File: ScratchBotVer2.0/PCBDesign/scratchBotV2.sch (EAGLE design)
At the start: 55 parts, among them T1 BD139, T3 BD139, U1 LM358M/NOPB, U2 LM358M/NOPB, U3 TCRT5000, U4 TCRT5000

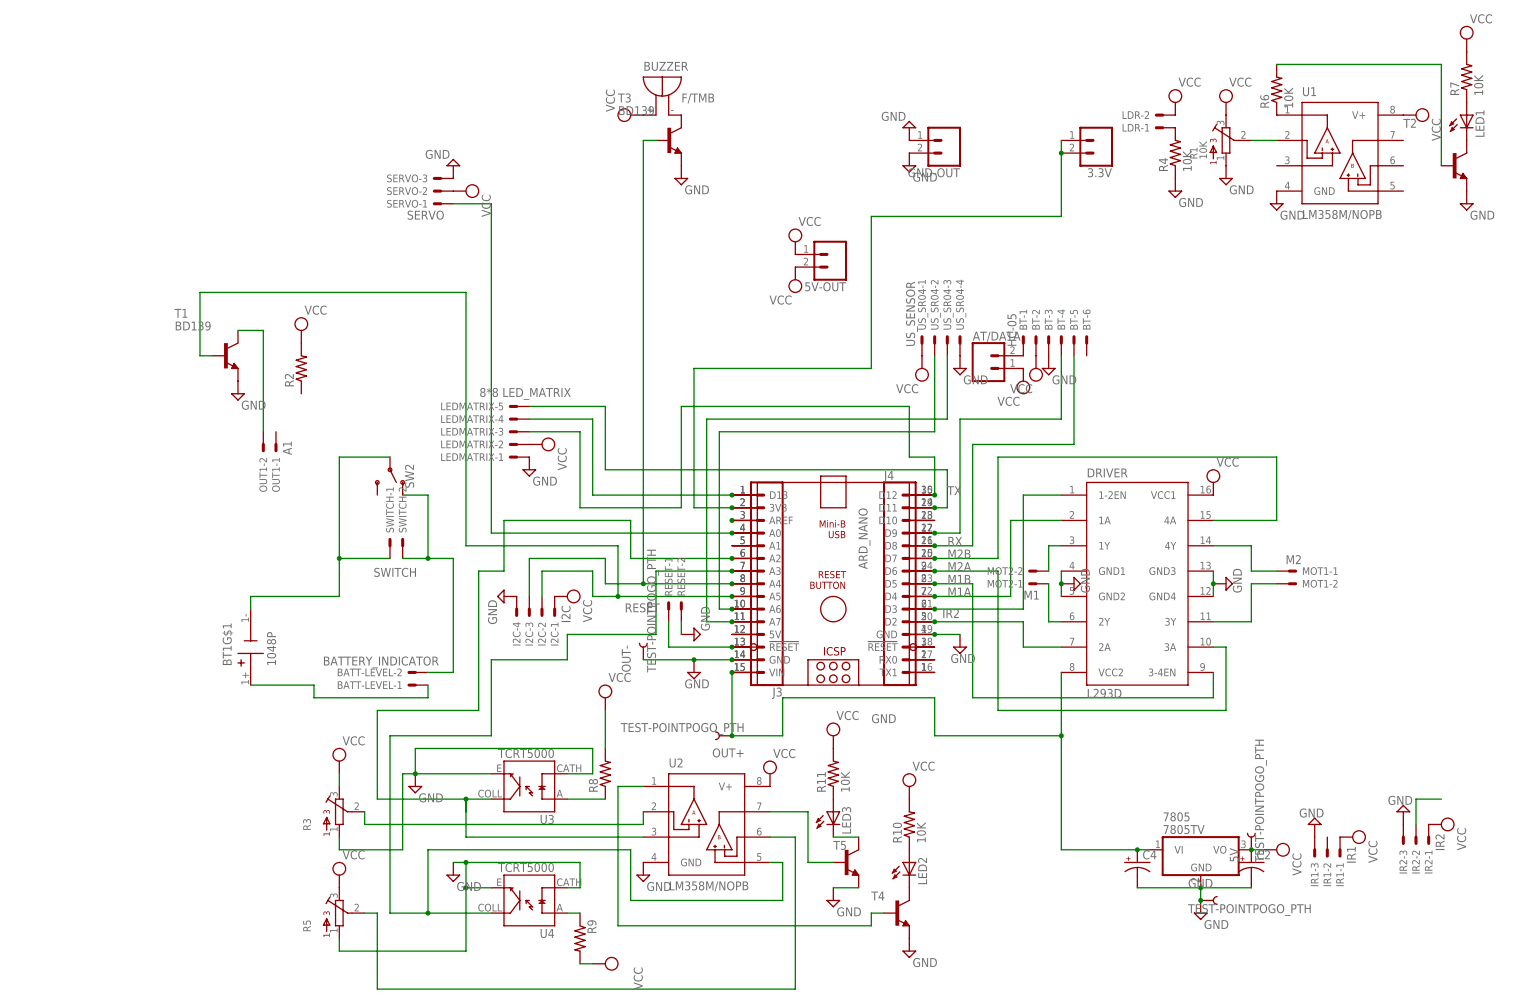
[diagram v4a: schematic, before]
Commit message: Output Pins of TCR5000 and LDR is connected to the analog pin of Arduino and reviewed the circuit.
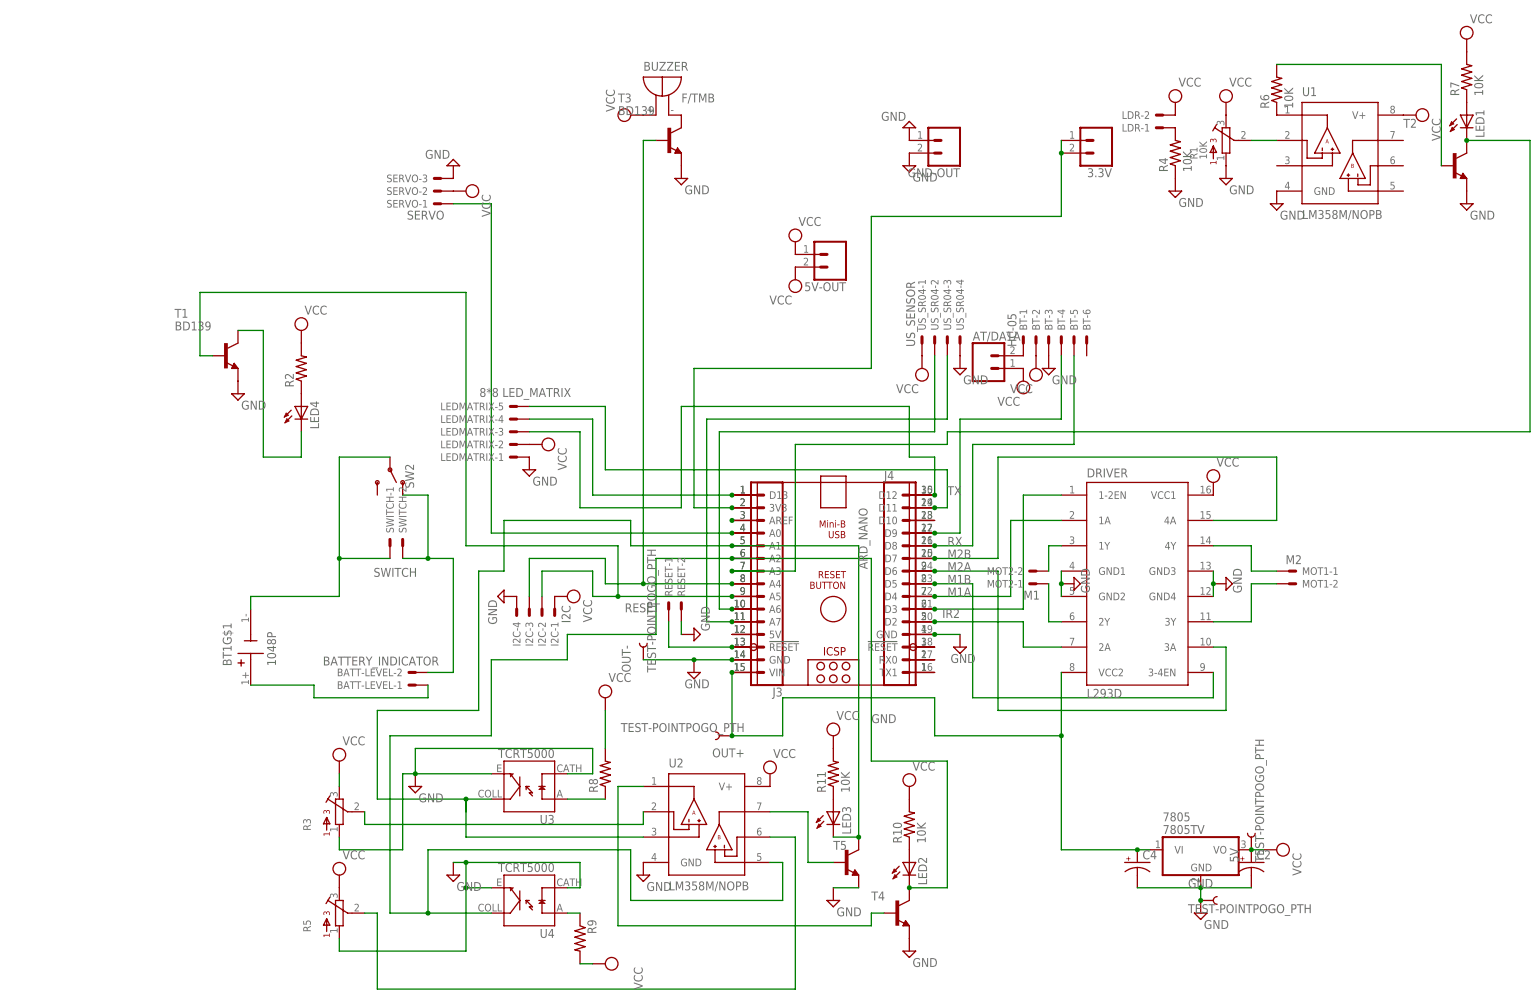
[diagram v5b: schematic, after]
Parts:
- removed IR1: IR1, Rembrandt Electronics - JST XH Connectors v1-0 (1):JST-XH-03-PIN-LONG-PAD
- removed IR2: IR2, Rembrandt Electronics - JST XH Connectors v1-0 (1):JST-XH-03-PIN-LONG-PAD
- removed OUT1: A1, Rembrandt Electronics - JST XH Connectors v1-0 (1):JST-XH-02-PIN-LONG-PAD
- added LED4: (no value), adafruit:LEDCHIPLED_1206
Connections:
- removed net N$30: LED2.C, T4.C
- removed net N$40: IR2-2.S
- removed net N$41: ARD_NANO.A3, J3.7, U2.+INB, U4.COLL
- removed net N$46: LED3.C, T5.C
- new net N$49: LED4.A, R2.1
- net GND: no longer IR1-3.S, IR2-3.S
- net N$15: now also ARD_NANO.A3, J3.7, LED1.C, T2.C; no longer ARD_NANO.A1, J3.5
- net N$16: now also ARD_NANO.A1, J3.5, LED3.C, T5.C; no longer ARD_NANO.A2, J3.6
- net N$17: now also LED4.C; no longer OUT1-2.S
- net N$32: now also ARD_NANO.A2, J3.6, LED2.C, T4.C, U2.+INB, U4.COLL; no longer LED1.C, T2.C
- net VCC: no longer IR1-1.S, IR2-1.S

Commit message: Resistors value updated
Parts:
- R10, R11: value 10K -> 100E
- R3, R5: value (none) -> 10K
- R7: value 10K -> 330 ohm
- R8, R9: value (none) -> 150 ohm
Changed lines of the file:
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@@
 <part name="U2" library="LM358M_NOPB" deviceset="LM358M/NOPB" device=""/>
 <part name="R1" library="bourns" deviceset="3362" device="H" value="10K"/>
-<part name="R3" library="bourns" deviceset="3362" device="H"/>
+<part name="R3" library="bourns" deviceset="3362" device="H" value="10K"/>
 <part name="SUPPLY32" library="supply2" library_urn="urn:adsk.eagle:library:372" deviceset="GND" device=""/>
 <part name="SUPPLY33" library="supply2" library_urn="urn:adsk.eagle:library:372" deviceset="VCC" device=""/>
@@
 <part name="SUPPLY38" library="supply2" library_urn="urn:adsk.eagle:library:372" deviceset="GND" device=""/>
 <part name="LED1" library="adafruit" deviceset="LED" device="CHIPLED_1206"/>
-<part name="R7" library="adafruit" deviceset="R-US_" device="M1206" value="10K"/>
+<part name="R7" library="adafruit" deviceset="R-US_" device="M1206" value="330 ohm"/>
 <part name="SUPPLY39" library="supply2" library_urn="urn:adsk.eagle:library:372" deviceset="VCC" device=""/>
 <part name="SUPPLY19" library="supply2" library_urn="urn:adsk.eagle:library:372" deviceset="GND" device=""/>
@@
 <part name="U4" library="TCRT5000" deviceset="TCRT5000" device=""/>
 <part name="SUPPLY40" library="supply2" library_urn="urn:adsk.eagle:library:372" deviceset="GND" device=""/>
-<part name="R8" library="adafruit" deviceset="R-US_" device="M1206"/>
+<part name="R8" library="adafruit" deviceset="R-US_" device="M1206" value="150 ohm"/>
 <part name="SUPPLY41" library="supply2" library_urn="urn:adsk.eagle:library:372" deviceset="VCC" device=""/>
-<part name="R9" library="adafruit" deviceset="R-US_" device="M1206"/>
+<part name="R9" library="adafruit" deviceset="R-US_" device="M1206" value="150 ohm"/>
 <part name="SUPPLY42" library="supply2" library_urn="urn:adsk.eagle:library:372" deviceset="VCC" device=""/>
 <part name="SUPPLY43" library="supply2" library_urn="urn:adsk.eagle:library:372" deviceset="GND" device=""/>
 <part name="SUPPLY44" library="supply2" library_urn="urn:adsk.eagle:library:372" deviceset="GND" device=""/>
 <part name="LED2" library="adafruit" deviceset="LED" device="CHIPLED_1206"/>
-<part name="R10" library="adafruit" deviceset="R-US_" device="M1206" value="10K"/>
+<part name="R10" library="adafruit" deviceset="R-US_" device="M1206" value="100E"/>
 <part name="SUPPLY45" library="supply2" library_urn="urn:adsk.eagle:library:372" deviceset="VCC" device=""/>
 <part name="SUPPLY46" library="supply2" library_urn="urn:adsk.eagle:library:372" deviceset="GND" device=""/>
@@
 <part name="SUPPLY48" library="supply2" library_urn="urn:adsk.eagle:library:372" deviceset="GND" device=""/>
 <part name="LED3" library="adafruit" deviceset="LED" device="CHIPLED_1206"/>
-<part name="R11" library="adafruit" deviceset="R-US_" device="M1206" value="10K"/>
+<part name="R11" library="adafruit" deviceset="R-US_" device="M1206" value="100E"/>
 <part name="SUPPLY49" library="supply2" library_urn="urn:adsk.eagle:library:372" deviceset="VCC" device=""/>
-<part name="R5" library="bourns" deviceset="3362" device="H"/>
+<part name="R5" library="bourns" deviceset="3362" device="H" value="10K"/>
 <part name="SUPPLY50" library="supply2" library_urn="urn:adsk.eagle:library:372" deviceset="VCC" device=""/>
 <part name="SUPPLY51" library="supply2" library_urn="urn:adsk.eagle:library:372" deviceset="VCC" device=""/>

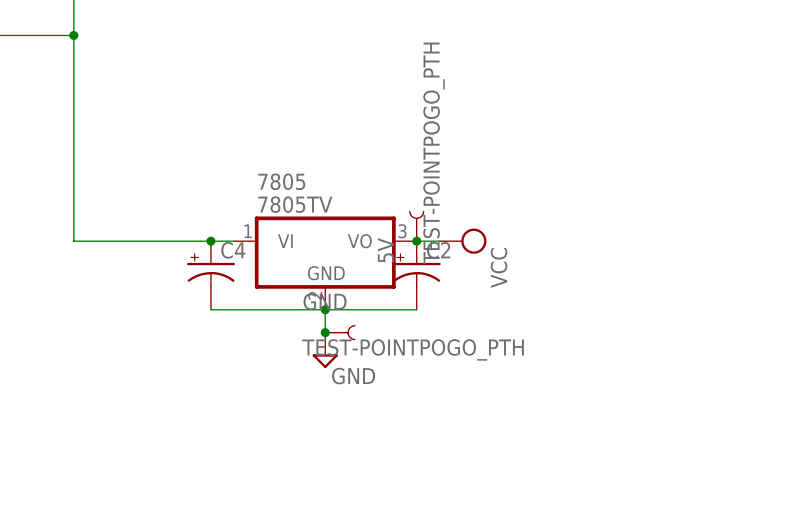
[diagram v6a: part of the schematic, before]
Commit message: component placement
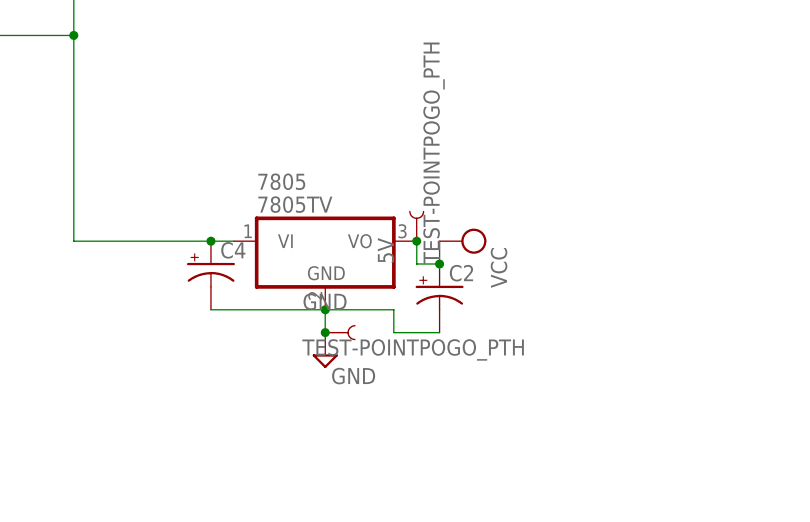
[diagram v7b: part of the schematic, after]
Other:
- moved on the sheet: C2
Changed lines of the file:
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@@
 <attribute name="VALUE" x="142.24" y="3.175" size="1.778" layer="96"/>
 </instance>
-<instance part="C2" gate="G$1" x="160.02" y="-2.54" smashed="yes">
-<attribute name="NAME" x="161.036" y="-1.905" size="1.778" layer="95"/>
-<attribute name="VALUE" x="161.036" y="-6.731" size="1.778" layer="96"/>
+<instance part="C2" gate="G$1" x="162.56" y="-5.08" smashed="yes">
+<attribute name="NAME" x="163.576" y="-4.445" size="1.778" layer="95"/>
+<attribute name="VALUE" x="163.576" y="-9.271" size="1.778" layer="96"/>
 </instance>
 <instance part="C4" gate="G$1" x="137.16" y="-2.54" smashed="yes">
@@
 <pinref part="SUPPLY12" gate="GND" pin="GND"/>
 <wire x1="149.86" y1="-10.16" x2="149.86" y2="-7.62" width="0.1524" layer="91"/>
-<wire x1="149.86" y1="-7.62" x2="160.02" y2="-7.62" width="0.1524" layer="91"/>
 <wire x1="137.16" y1="-7.62" x2="149.86" y2="-7.62" width="0.1524" layer="91"/>
 <junction x="149.86" y="-7.62"/>
@@
 <pinref part="GND" gate="G$1" pin="1"/>
 <junction x="149.86" y="-10.16"/>
+<wire x1="149.86" y1="-7.62" x2="157.48" y2="-7.62" width="0.1524" layer="91"/>
+<wire x1="157.48" y1="-7.62" x2="157.48" y2="-10.16" width="0.1524" layer="91"/>
+<wire x1="157.48" y1="-10.16" x2="162.56" y2="-10.16" width="0.1524" layer="91"/>
 </segment>
 <segment>
@@
 </segment>
 <segment>
-<pinref part="SUPPLY3" gate="G$1" pin="VCC"/>
-<pinref part="7805" gate="A1" pin="VO"/>
-<pinref part="C2" gate="G$1" pin="+"/>
-<junction x="160.02" y="0"/>
-<wire x1="160.02" y1="0" x2="162.56" y2="0" width="0.1524" layer="91"/>
-<pinref part="5V" gate="G$1" pin="1"/>
-</segment>
-<segment>
 <pinref part="SUPPLY16" gate="G$1" pin="VCC"/>
 <pinref part="BT" gate="-2" pin="S"/>
@@
 <pinref part="SUPPLY51" gate="G$1" pin="VCC"/>
 </segment>
-</net>
+<segment>
+<pinref part="C2" gate="G$1" pin="+"/>
+<pinref part="SUPPLY3" gate="G$1" pin="VCC"/>
+<wire x1="162.56" y1="-2.54" x2="162.56" y2="0" width="0.1524" layer="91"/>
+<wire x1="162.56" y1="-2.54" x2="160.02" y2="-2.54" width="0.1524" layer="91"/>
+<junction x="162.56" y="-2.54"/>
+<pinref part="7805" gate="A1" pin="VO"/>
+<pinref part="5V" gate="G$1" pin="1"/>
+<wire x1="160.02" y1="-2.54" x2="160.02" y2="0" width="0.1524" layer="91"/>
+<junction x="160.02" y="0"/>
+</segment>
+</net>
